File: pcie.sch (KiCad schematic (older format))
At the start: 9 parts, among them U2 PCIE-064-02

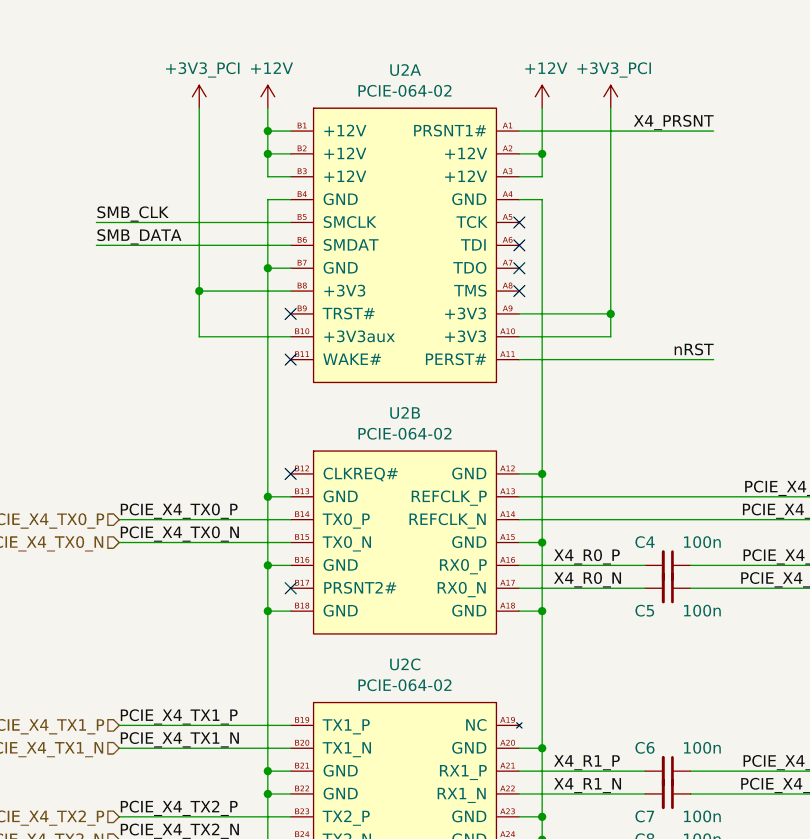
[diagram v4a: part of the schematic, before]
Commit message: lib, sch: Fix connectors refdes letter
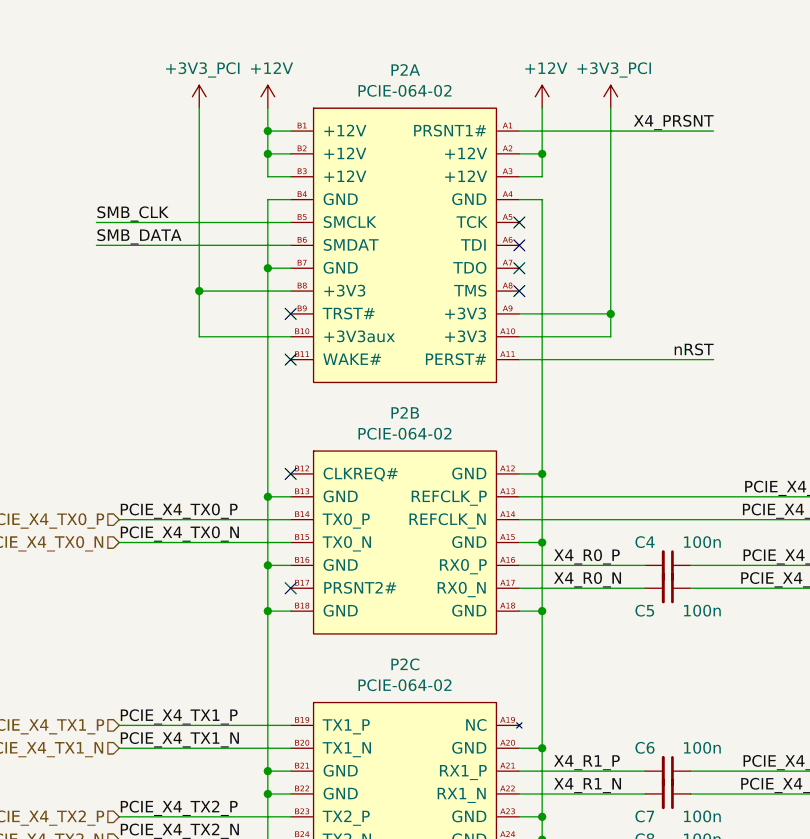
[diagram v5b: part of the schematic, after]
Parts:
- renumbered U2 to P2
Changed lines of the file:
@@
 $EndDescr
 $Comp
-L pimouss-motherboard:PCIE-064-02 U2
+L pimouss-motherboard:PCIE-064-02 P2
 U 1 1 5C978539
 P 8000 1500
-F 0 "U2" H 8400 1665 50  0000 C CNN
+F 0 "P2" H 8400 1665 50  0000 C CNN
 F 1 "PCIE-064-02" H 8400 1574 50  0000 C CNN
 F 2 "pimouss-motherboard:SAMTEC_PCIE-064-02-F-D-TH" H 7900 1550 50  0001 C CNN
@@
 $EndComp
 $Comp
-L pimouss-motherboard:PCIE-064-02 U2
+L pimouss-motherboard:PCIE-064-02 P2
 U 2 1 5C978540
 P 8000 3000
-F 0 "U2" H 8400 3165 50  0000 C CNN
+F 0 "P2" H 8400 3165 50  0000 C CNN
 F 1 "PCIE-064-02" H 8400 3074 50  0000 C CNN
 F 2 "pimouss-motherboard:SAMTEC_PCIE-064-02-F-D-TH" H 7900 3050 50  0001 C CNN
@@
 $EndComp
 $Comp
-L pimouss-motherboard:PCIE-064-02 U2
+L pimouss-motherboard:PCIE-064-02 P2
 U 3 1 5C978547
 P 8000 4100
-F 0 "U2" H 8400 4265 50  0000 C CNN
+F 0 "P2" H 8400 4265 50  0000 C CNN
 F 1 "PCIE-064-02" H 8400 4174 50  0000 C CNN
 F 2 "pimouss-motherboard:SAMTEC_PCIE-064-02-F-D-TH" H 7900 4150 50  0001 C CNN

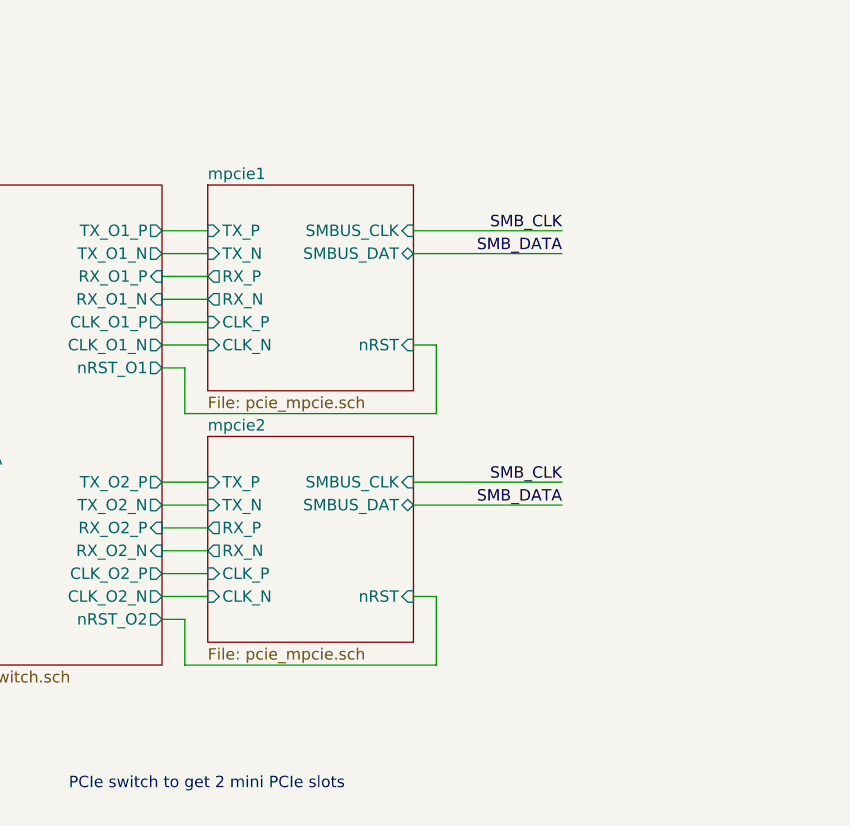
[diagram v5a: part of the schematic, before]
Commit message: sch: Add names to ALL PCIe nets
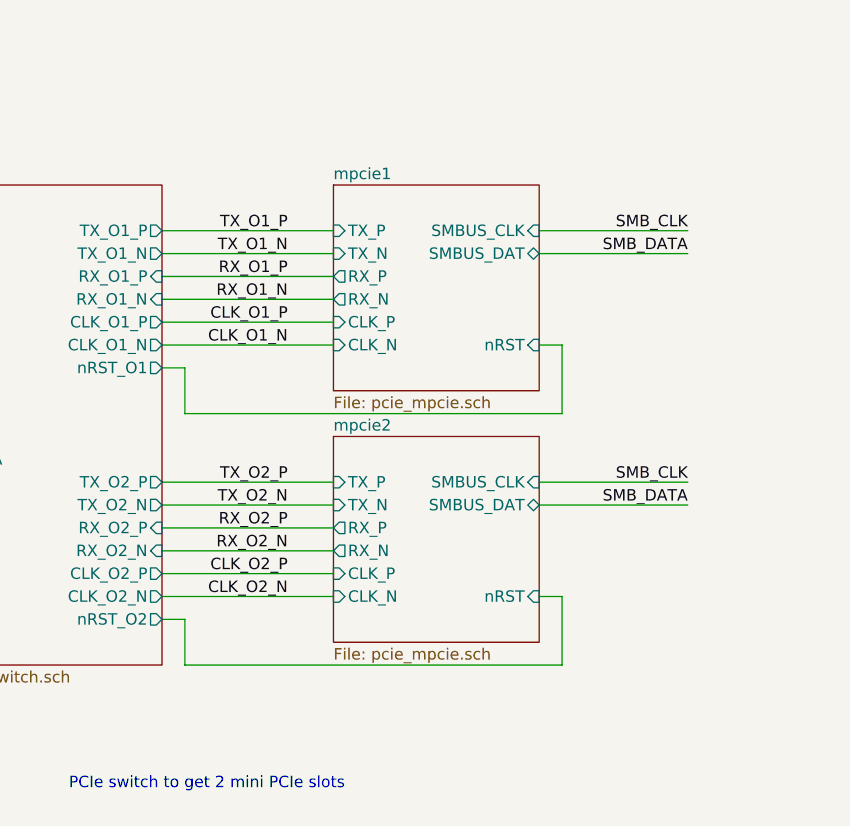
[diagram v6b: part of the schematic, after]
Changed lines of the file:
@@
 $EndSheet
 $Sheet
-S 3600 3100 900  900
+S 4150 3100 900  900
 U 5D489567
 F0 "mpcie1" 50
 F1 "pcie_mpcie.sch" 50
-F2 "TX_P" I L 3600 3300 50
-F3 "TX_N" I L 3600 3400 50
-F4 "RX_P" O L 3600 3500 50
-F5 "RX_N" O L 3600 3600 50
-F6 "CLK_P" I L 3600 3700 50
-F7 "CLK_N" I L 3600 3800 50
-F8 "SMBUS_CLK" I R 4500 3300 50
-F9 "SMBUS_DAT" B R 4500 3400 50
-F10 "nRST" I R 4500 3800 50
+F2 "TX_P" I L 4150 3300 50
+F3 "TX_N" I L 4150 3400 50
+F4 "RX_P" O L 4150 3500 50
+F5 "RX_N" O L 4150 3600 50
+F6 "CLK_P" I L 4150 3700 50
+F7 "CLK_N" I L 4150 3800 50
+F8 "SMBUS_CLK" I R 5050 3300 50
+F9 "SMBUS_DAT" B R 5050 3400 50
+F10 "nRST" I R 5050 3800 50
 $EndSheet
 $Sheet
-S 3600 4200 900  900
+S 4150 4200 900  900
 U 5D9F9D59
 F0 "mpcie2" 50
 F1 "pcie_mpcie.sch" 50
-F2 "TX_P" I L 3600 4400 50
-F3 "TX_N" I L 3600 4500 50
-F4 "RX_P" O L 3600 4600 50
-F5 "RX_N" O L 3600 4700 50
-F6 "CLK_P" I L 3600 4800 50
-F7 "CLK_N" I L 3600 4900 50
-F8 "SMBUS_CLK" I R 4500 4400 50
-F9 "SMBUS_DAT" B R 4500 4500 50
-F10 "nRST" I R 4500 4900 50
+F2 "TX_P" I L 4150 4400 50
+F3 "TX_N" I L 4150 4500 50
+F4 "RX_P" O L 4150 4600 50
+F5 "RX_N" O L 4150 4700 50
+F6 "CLK_P" I L 4150 4800 50
+F7 "CLK_N" I L 4150 4900 50
+F8 "SMBUS_CLK" I R 5050 4400 50
+F9 "SMBUS_DAT" B R 5050 4500 50
+F10 "nRST" I R 5050 4900 50
 $EndSheet
 Wire Wire Line
-	3400 3300 3600 3300
-Wire Wire Line
-	3400 3400 3600 3400
-Wire Wire Line
-	3400 3500 3600 3500
-Wire Wire Line
-	3400 3600 3600 3600
-Wire Wire Line
-	3400 3700 3600 3700
-Wire Wire Line
-	3400 3800 3600 3800
-Wire Wire Line
-	3400 4400 3600 4400
-Wire Wire Line
-	3400 4500 3600 4500
-Wire Wire Line
-	3400 4600 3600 4600
-Wire Wire Line
-	3400 4700 3600 4700
-Wire Wire Line
-	3400 4800 3600 4800
-Wire Wire Line
-	3400 4900 3600 4900
+	3400 3300 4150 3300
+Wire Wire Line
+	3400 3400 4150 3400
+Wire Wire Line
+	3400 3500 4150 3500
+Wire Wire Line
+	3400 3600 4150 3600
+Wire Wire Line
+	3400 3700 4150 3700
+Wire Wire Line
+	3400 3800 4150 3800
+Wire Wire Line
+	3400 4400 4150 4400
+Wire Wire Line
+	3400 4500 4150 4500
+Wire Wire Line
+	3400 4600 4150 4600
+Wire Wire Line
+	3400 4700 4150 4700
+Wire Wire Line
+	3400 4800 4150 4800
+Wire Wire Line
+	3400 4900 4150 4900
 Wire Wire Line
 	3400 3900 3500 3900
@@
 	3500 3900 3500 4100
 Wire Wire Line
-	3500 4100 4600 4100
-Wire Wire Line
-	4600 4100 4600 3800
-Wire Wire Line
-	4600 3800 4500 3800
+	3500 4100 5150 4100
+Wire Wire Line
+	5150 4100 5150 3800
+Wire Wire Line
+	5150 3800 5050 3800
 Wire Wire Line
 	3400 5000 3500 5000
@@
 	3500 5000 3500 5200
 Wire Wire Line
-	3500 5200 4600 5200
-Wire Wire Line
-	4600 5200 4600 4900
-Wire Wire Line
-	4600 4900 4500 4900
+	3500 5200 5150 5200
+Wire Wire Line
+	5150 5200 5150 4900
+Wire Wire Line
+	5150 4900 5050 4900
 Wire Wire Line
 	1650 4000 2300 4000
@@
 SMB_DATA
 Wire Wire Line
-	5150 3300 4500 3300
-Wire Wire Line
-	5150 3400 4500 3400
-Text Label 5150 3300 2    50   ~ 0
-SMB_CLK
-Text Label 5150 3400 2    50   ~ 0
-SMB_DATA
-Wire Wire Line
-	5150 4400 4500 4400
-Wire Wire Line
-	5150 4500 4500 4500
-Text Label 5150 4400 2    50   ~ 0
-SMB_CLK
-Text Label 5150 4500 2    50   ~ 0
+	5700 3300 5050 3300
+Wire Wire Line
+	5700 3400 5050 3400
+Text Label 5700 3300 2    50   ~ 0
+SMB_CLK
+Text Label 5700 3400 2    50   ~ 0
+SMB_DATA
+Wire Wire Line
+	5700 4400 5050 4400
+Wire Wire Line
+	5700 4500 5050 4500
+Text Label 5700 4400 2    50   ~ 0
+SMB_CLK
+Text Label 5700 4500 2    50   ~ 0
 SMB_DATA
 Wire Wire Line
@@
 Text Label 2200 1300 2    50   ~ 0
 SMB_DATA
+Text Label 3950 3500 2    50   ~ 0
+RX_O1_P
+Text Label 3950 3600 2    50   ~ 0
+RX_O1_N
+Text Label 3950 3300 2    50   ~ 0
+TX_O1_P
+Text Label 3950 3400 2    50   ~ 0
+TX_O1_N
+Text Label 3950 3700 2    50   ~ 0
+CLK_O1_P
+Text Label 3950 3800 2    50   ~ 0
+CLK_O1_N
+Text Label 3950 4400 2    50   ~ 0
+TX_O2_P
+Text Label 3950 4500 2    50   ~ 0
+TX_O2_N
+Text Label 3950 4600 2    50   ~ 0
+RX_O2_P
+Text Label 3950 4700 2    50   ~ 0
+RX_O2_N
+Text Label 3950 4800 2    50   ~ 0
+CLK_O2_P
+Text Label 3950 4900 2    50   ~ 0
+CLK_O2_N
 $EndSCHEMATC
